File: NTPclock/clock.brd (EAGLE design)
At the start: 115 x 85 mm, 28 parts, among them IC1 MAX7219CNG

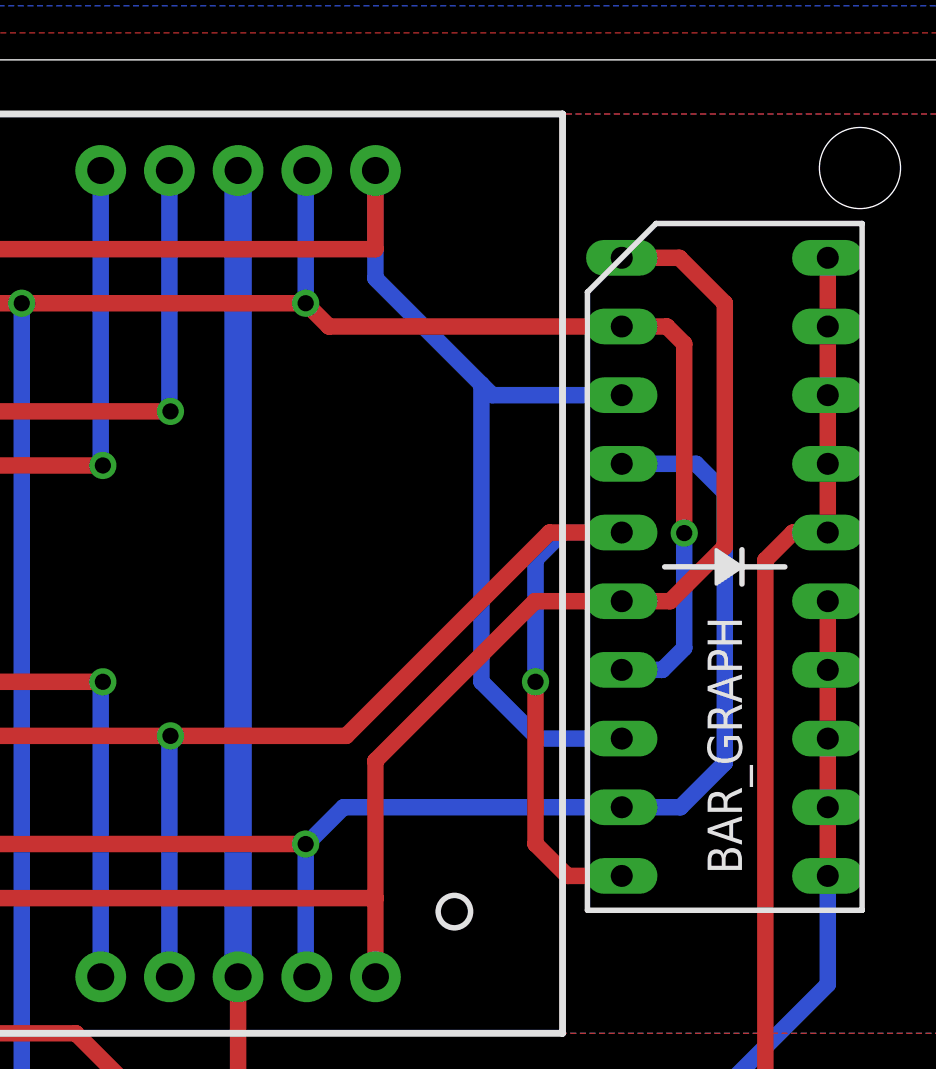
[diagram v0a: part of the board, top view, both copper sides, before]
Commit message: Correct bar graph ordering
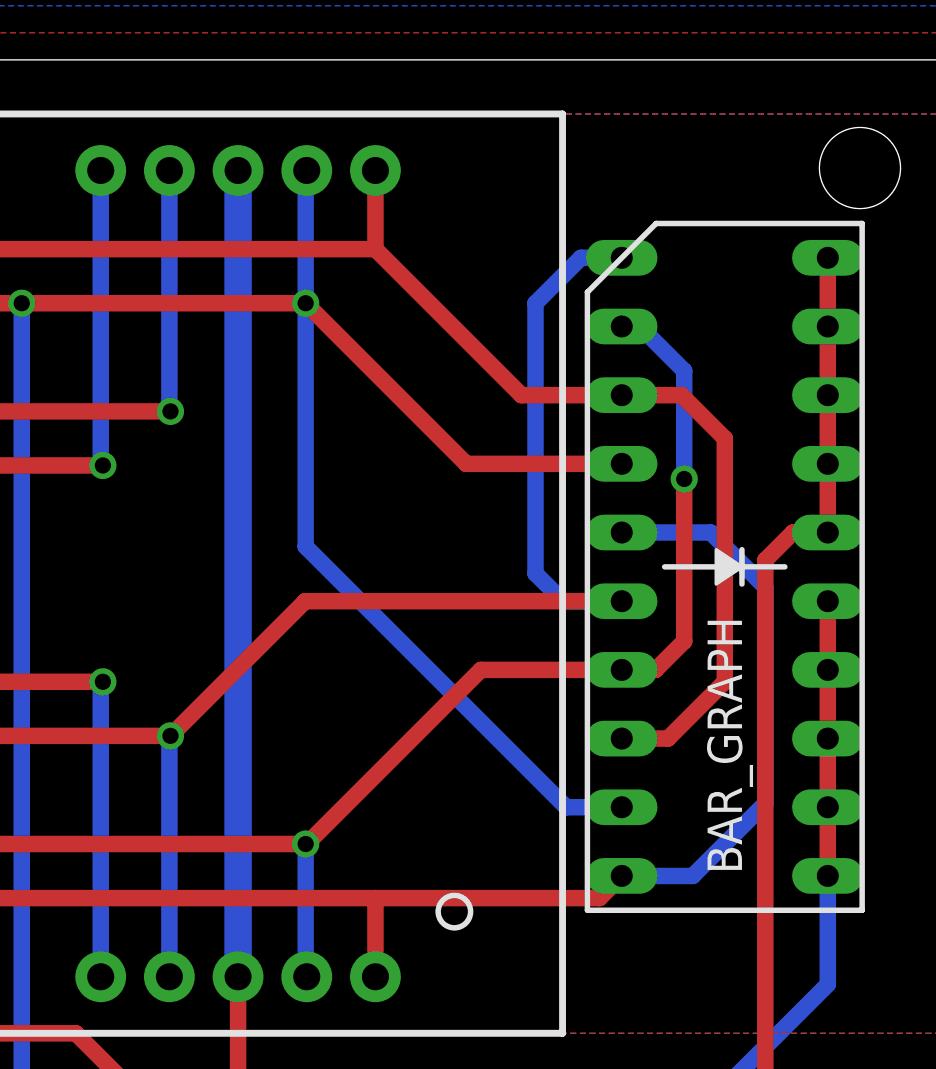
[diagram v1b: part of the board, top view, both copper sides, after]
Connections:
- net A: now also BAR_GRAPH.4, BAR_GRAPH.9; no longer BAR_GRAPH.2, BAR_GRAPH.7
- net C: now also BAR_GRAPH.2, BAR_GRAPH.7; no longer BAR_GRAPH.4, BAR_GRAPH.9
- net D: now also BAR_GRAPH.1, BAR_GRAPH.6; no longer BAR_GRAPH.10, BAR_GRAPH.5
- net DP: now also BAR_GRAPH.10, BAR_GRAPH.5; no longer BAR_GRAPH.1, BAR_GRAPH.6
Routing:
- net A: track 156.0 -> 166.3 mm, vias 5 -> 4
- net DP: track 134.7 -> 129.9 mm
- net B: track 155.4 -> 152.3 mm
- net D: track 157.5 -> 156.2 mm, vias 4 -> 3
- net C: track 134.1 -> 133.3 mm, vias 3 -> 4
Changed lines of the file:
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@@
 <contactref element="DIG_0" pad="7"/>
 <contactref element="IC1" pad="14"/>
-<contactref element="BAR_GRAPH" pad="2"/>
-<contactref element="BAR_GRAPH" pad="7"/>
 <wire x1="19.45" y1="76" x2="38.5" y2="76" width="0.6096" layer="1"/>
 <wire x1="38.5" y1="76" x2="66.5" y2="76" width="0.6096" layer="1"/>
@@
 <wire x1="80" y1="44" x2="80" y2="76" width="0.6096" layer="16"/>
 <via x="80" y="76" extent="1-16" drill="0.6" diameter="0.8"/>
-<wire x1="91.36" y1="75.14" x2="102.19" y2="75.14" width="0.6096" layer="1"/>
-<wire x1="102.19" y1="75.14" x2="103.86" y2="75.14" width="0.6096" layer="1"/>
-<wire x1="103.86" y1="75.14" x2="104.5" y2="74.5" width="0.6096" layer="1"/>
-<wire x1="104.5" y1="74.5" x2="104.5" y2="67.5" width="0.6096" layer="1"/>
-<via x="104.5" y="67.5" extent="1-16" drill="0.6" diameter="0.8"/>
-<wire x1="104.5" y1="67.5" x2="104.5" y2="63.25" width="0.6096" layer="16"/>
-<wire x1="104.5" y1="63.25" x2="103.69" y2="62.44" width="0.6096" layer="16"/>
-<wire x1="103.69" y1="62.44" x2="102.19" y2="62.44" width="0.6096" layer="16"/>
-<wire x1="91.36" y1="75.14" x2="90.5" y2="76" width="0.6096" layer="1"/>
 <via x="90.5" y="76" extent="1-16" drill="0.6"/>
 <wire x1="90.5" y1="76" x2="90.5" y2="80.87" width="0.6096" layer="16"/>
 <wire x1="90.5" y1="80.87" x2="90.54" y2="80.91" width="0.6096" layer="16"/>
+<contactref element="BAR_GRAPH" pad="9"/>
+<contactref element="BAR_GRAPH" pad="4"/>
+<wire x1="90.5" y1="76" x2="96.44" y2="70.06" width="0.6096" layer="1"/>
+<wire x1="96.44" y1="70.06" x2="102.19" y2="70.06" width="0.6096" layer="1"/>
+<wire x1="90.5" y1="67" x2="90.5" y2="76" width="0.6096" layer="16"/>
+<wire x1="102.19" y1="57.36" x2="100.14" y2="57.36" width="0.6096" layer="16"/>
+<wire x1="100.14" y1="57.36" x2="90.5" y2="67" width="0.6096" layer="16"/>
 </signal>
 <signal name="B">
@@
 <contactref element="DIG_0" pad="6"/>
 <contactref element="IC1" pad="16"/>
-<contactref element="BAR_GRAPH" pad="3"/>
-<contactref element="BAR_GRAPH" pad="8"/>
 <wire x1="19.99" y1="78" x2="41.08" y2="78" width="0.6096" layer="1"/>
 <wire x1="41.08" y1="78" x2="69.08" y2="78" width="0.6096" layer="1"/>
@@
 <wire x1="76" y1="45" x2="76" y2="78" width="0.6096" layer="16"/>
 <via x="76" y="78" extent="1-16" drill="0.6" diameter="0.8"/>
-<wire x1="102.19" y1="72.6" x2="97.4" y2="72.6" width="0.6096" layer="16"/>
-<wire x1="97.4" y1="72.6" x2="97" y2="73" width="0.6096" layer="16"/>
-<wire x1="97" y1="73" x2="93.08" y2="76.92" width="0.6096" layer="16"/>
-<wire x1="93.08" y1="76.92" x2="93.08" y2="80.91" width="0.6096" layer="16"/>
-<wire x1="102.19" y1="72.6" x2="101.6" y2="72.6" width="0.6096" layer="16"/>
-<wire x1="102.19" y1="59.9" x2="99.1" y2="59.9" width="0.6096" layer="16"/>
-<wire x1="99.1" y1="59.9" x2="97" y2="62" width="0.6096" layer="16"/>
-<wire x1="97" y1="62" x2="97" y2="73" width="0.6096" layer="16"/>
+<contactref element="BAR_GRAPH" pad="8"/>
+<contactref element="BAR_GRAPH" pad="3"/>
+<wire x1="93.08" y1="78" x2="98.48" y2="72.6" width="0.6096" layer="1"/>
+<wire x1="98.48" y1="72.6" x2="102.19" y2="72.6" width="0.6096" layer="1"/>
+<wire x1="102.19" y1="59.9" x2="103.9" y2="59.9" width="0.6096" layer="1"/>
+<wire x1="103.9" y1="59.9" x2="106" y2="62" width="0.6096" layer="1"/>
+<wire x1="104.4" y1="72.6" x2="102.19" y2="72.6" width="0.6096" layer="1"/>
+<wire x1="106" y1="62" x2="106" y2="71" width="0.6096" layer="1"/>
+<wire x1="106" y1="71" x2="104.4" y2="72.6" width="0.6096" layer="1"/>
 </signal>
 <signal name="C">
@@
 <contactref element="DIG_0" pad="4"/>
 <contactref element="IC1" pad="20"/>
-<contactref element="BAR_GRAPH" pad="4"/>
-<contactref element="BAR_GRAPH" pad="9"/>
 <wire x1="14.54" y1="51.09" x2="19.45" y2="56" width="0.6096" layer="1"/>
 <wire x1="19.45" y1="56" x2="38.5" y2="56" width="0.6096" layer="1"/>
@@
 <wire x1="64.97" y1="44.97" x2="66.54" y2="46.54" width="0.6096" layer="16"/>
 <wire x1="66.54" y1="46.54" x2="66.54" y2="51.09" width="0.6096" layer="16"/>
-<wire x1="91.9" y1="57.36" x2="102.19" y2="57.36" width="0.6096" layer="16"/>
-<wire x1="102.19" y1="70.06" x2="104.94" y2="70.06" width="0.6096" layer="16"/>
-<wire x1="104.94" y1="70.06" x2="106" y2="69" width="0.6096" layer="16"/>
-<wire x1="106" y1="69" x2="106" y2="59" width="0.6096" layer="16"/>
-<wire x1="106" y1="59" x2="104.36" y2="57.36" width="0.6096" layer="16"/>
-<wire x1="104.36" y1="57.36" x2="102.19" y2="57.36" width="0.6096" layer="16"/>
 <wire x1="90.54" y1="51.09" x2="90.5" y2="51.09" width="0.6096" layer="16"/>
 <wire x1="90.5" y1="51.09" x2="90.5" y2="56" width="0.6096" layer="16"/>
 <wire x1="90.5" y1="56" x2="90.54" y2="56" width="0.6096" layer="16"/>
-<wire x1="90.54" y1="56" x2="91.9" y2="57.36" width="0.6096" layer="16"/>
 <wire x1="66.5" y1="56" x2="90.5" y2="56" width="0.6096" layer="1"/>
 <via x="90.5" y="56" extent="1-16" drill="0.6"/>
+<contactref element="BAR_GRAPH" pad="7"/>
+<contactref element="BAR_GRAPH" pad="2"/>
+<wire x1="96.98" y1="62.44" x2="102.19" y2="62.44" width="0.6096" layer="1"/>
+<wire x1="102.19" y1="75.14" x2="102.86" y2="75.14" width="0.6096" layer="16"/>
+<wire x1="102.86" y1="75.14" x2="104.5" y2="73.5" width="0.6096" layer="16"/>
+<wire x1="104.5" y1="73.5" x2="104.5" y2="69.5" width="0.6096" layer="16"/>
+<via x="104.5" y="69.5" extent="1-16" drill="0.6"/>
+<wire x1="104.5" y1="69.5" x2="104.5" y2="63.5" width="0.6096" layer="1"/>
+<wire x1="104.5" y1="63.5" x2="103.44" y2="62.44" width="0.6096" layer="1"/>
+<wire x1="103.44" y1="62.44" x2="102.19" y2="62.44" width="0.6096" layer="1"/>
+<wire x1="96.98" y1="62.44" x2="90.54" y2="56" width="0.6096" layer="1"/>
+<wire x1="90.54" y1="56" x2="90.5" y2="56" width="0.6096" layer="1"/>
 </signal>
 <signal name="D">
@@
 <contactref element="DIG_0" pad="2"/>
 <contactref element="IC1" pad="23"/>
-<contactref element="BAR_GRAPH" pad="5"/>
-<contactref element="BAR_GRAPH" pad="10"/>
 <contactref element="D2" pad="A"/>
 <wire x1="9.46" y1="51.09" x2="18.37" y2="60" width="0.6096" layer="1"/>
@@
 <wire x1="57.35" y1="43.35" x2="61.46" y2="47.46" width="0.6096" layer="16"/>
 <wire x1="61.46" y1="47.46" x2="61.46" y2="51.09" width="0.6096" layer="16"/>
-<wire x1="92" y1="60" x2="85.5" y2="60" width="0.6096" layer="1"/>
-<wire x1="102.19" y1="67.52" x2="99.52" y2="67.52" width="0.6096" layer="1"/>
-<wire x1="99.52" y1="67.52" x2="92" y2="60" width="0.6096" layer="1"/>
-<wire x1="102.19" y1="54.82" x2="100.18" y2="54.82" width="0.6096" layer="1"/>
-<wire x1="100.18" y1="54.82" x2="99" y2="56" width="0.6096" layer="1"/>
-<wire x1="99" y1="56" x2="99" y2="62" width="0.6096" layer="1"/>
-<via x="99" y="62" extent="1-16" drill="0.6"/>
-<wire x1="99" y1="62" x2="99" y2="66.52" width="0.6096" layer="16"/>
-<wire x1="99" y1="66.52" x2="100" y2="67.52" width="0.6096" layer="16"/>
-<wire x1="100" y1="67.52" x2="102.19" y2="67.52" width="0.6096" layer="16"/>
+<contactref element="BAR_GRAPH" pad="6"/>
+<contactref element="BAR_GRAPH" pad="1"/>
+<wire x1="90.48" y1="64.98" x2="102.19" y2="64.98" width="0.6096" layer="1"/>
+<wire x1="85.5" y1="60" x2="90.48" y2="64.98" width="0.6096" layer="1"/>
+<wire x1="102.19" y1="77.68" x2="100.68" y2="77.68" width="0.6096" layer="16"/>
+<wire x1="100.68" y1="77.68" x2="99" y2="76" width="0.6096" layer="16"/>
+<wire x1="102.19" y1="64.98" x2="100.02" y2="64.98" width="0.6096" layer="16"/>
+<wire x1="100.02" y1="64.98" x2="99" y2="66" width="0.6096" layer="16"/>
+<wire x1="99" y1="66" x2="99" y2="76" width="0.6096" layer="16"/>
 </signal>
 <signal name="E">
@@
 <contactref element="DIG_0" pad="5"/>
 <contactref element="IC1" pad="22"/>
-<contactref element="BAR_GRAPH" pad="1"/>
-<contactref element="BAR_GRAPH" pad="6"/>
 <wire x1="17.08" y1="51.09" x2="19.99" y2="54" width="0.6096" layer="1"/>
 <wire x1="19.99" y1="54" x2="41.08" y2="54" width="0.6096" layer="1"/>
@@
 <wire x1="59.89" y1="46.11" x2="56.5" y2="49.5" width="0.6096" layer="1"/>
 <wire x1="56.5" y1="49.5" x2="56.5" y2="54" width="0.6096" layer="1"/>
-<wire x1="102.19" y1="64.98" x2="98.98" y2="64.98" width="0.6096" layer="1"/>
-<wire x1="98.98" y1="64.98" x2="93.08" y2="59.08" width="0.6096" layer="1"/>
-<wire x1="93.08" y1="59.08" x2="93.08" y2="54" width="0.6096" layer="1"/>
-<wire x1="102.19" y1="77.68" x2="104.32" y2="77.68" width="0.6096" layer="1"/>
-<wire x1="104.32" y1="77.68" x2="106" y2="76" width="0.6096" layer="1"/>
-<wire x1="106" y1="76" x2="106" y2="67" width="0.6096" layer="1"/>
-<wire x1="106" y1="67" x2="103.98" y2="64.98" width="0.6096" layer="1"/>
-<wire x1="103.98" y1="64.98" x2="102.19" y2="64.98" width="0.6096" layer="1"/>
+<contactref element="BAR_GRAPH" pad="10"/>
+<contactref element="BAR_GRAPH" pad="5"/>
+<wire x1="93.08" y1="54" x2="101.37" y2="54" width="0.6096" layer="1"/>
+<wire x1="101.37" y1="54" x2="102.19" y2="54.82" width="0.6096" layer="1"/>
+<wire x1="102.19" y1="54.82" x2="104.82" y2="54.82" width="0.6096" layer="16"/>
+<wire x1="104.82" y1="54.82" x2="107.5" y2="57.5" width="0.6096" layer="16"/>
+<wire x1="107.5" y1="65.5" x2="105.48" y2="67.52" width="0.6096" layer="16"/>
+<wire x1="105.48" y1="67.52" x2="102.19" y2="67.52" width="0.6096" layer="16"/>
+<wire x1="107.5" y1="57.5" x2="107.5" y2="65.5" width="0.6096" layer="16"/>
 </signal>
 <signal name="DIGIT7">
